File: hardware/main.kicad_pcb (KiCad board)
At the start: 2 copper layers, 60 x 40 mm, 4 parts

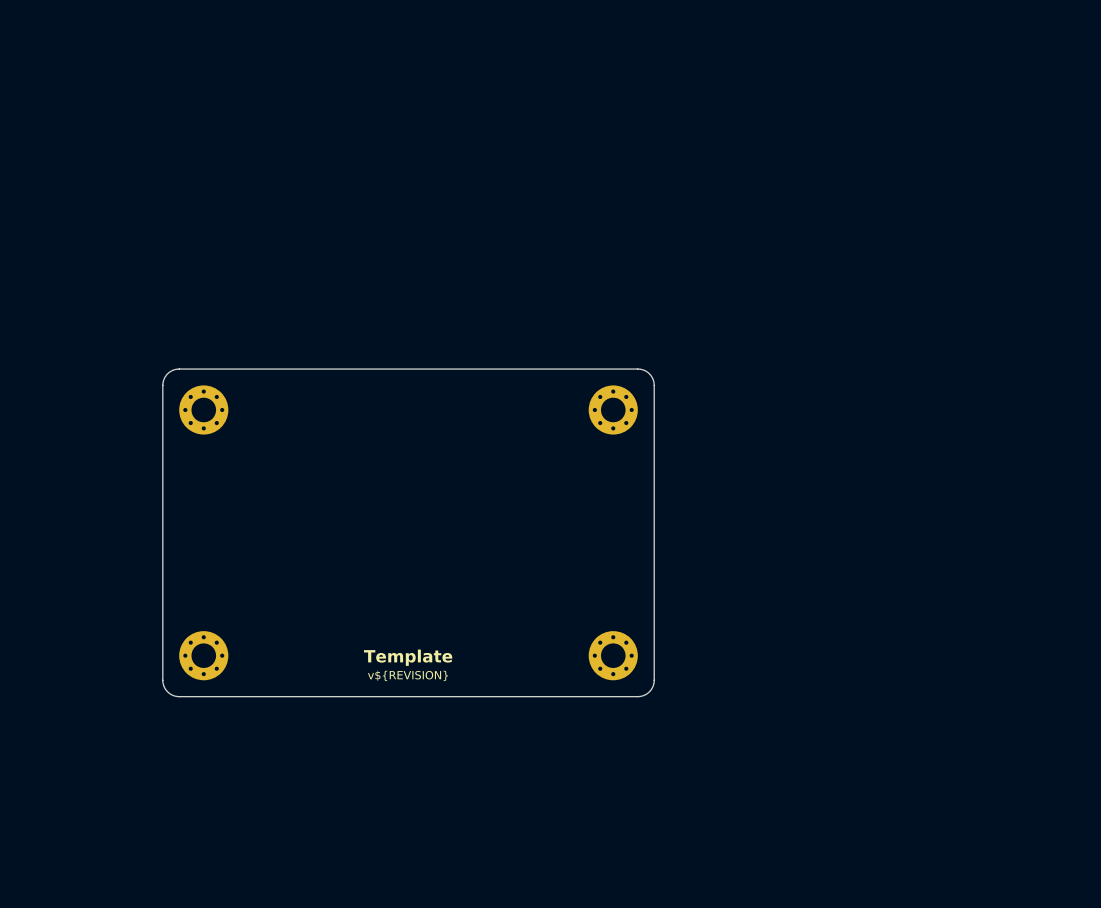
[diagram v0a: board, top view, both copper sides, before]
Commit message: add connectors and change through hole for HV
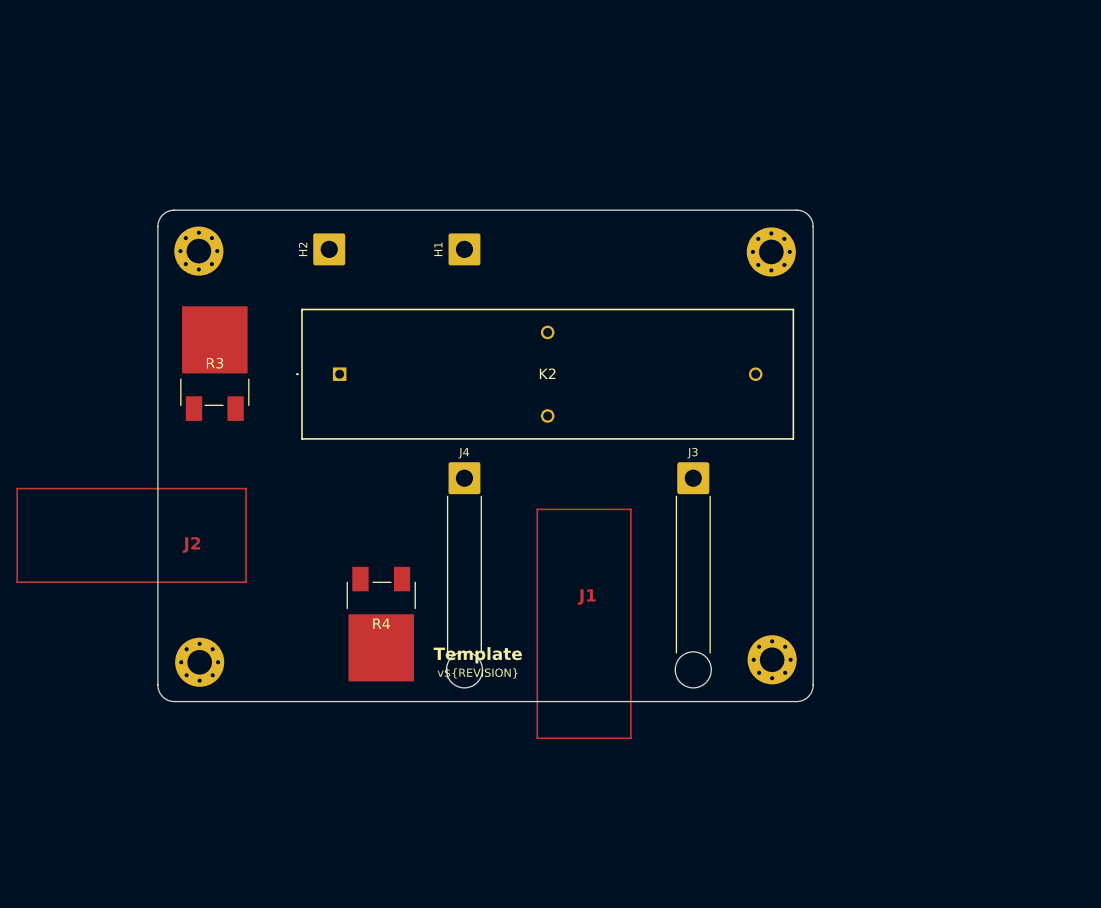
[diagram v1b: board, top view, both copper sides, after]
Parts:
- added H1: ~, Connector_Wire:SolderWire-1.5sqmm_1x01_D1.7mm_OD3.9mm, F.Cu at (152.8, 61.4)
- added H2: ~, Connector_Wire:SolderWire-1.5sqmm_1x01_D1.7mm_OD3.9mm, F.Cu at (136.3, 61.4)
- added J3: Strain_Relief_1, Connector_Wire:SolderWire-1.5sqmm_1x01_D1.7mm_OD3.9mm_Relief, F.Cu at (180.8, 89.3)
- added J4: Strain_Relief_2, Connector_Wire:SolderWire-1.5sqmm_1x01_D1.7mm_OD3.9mm_Relief, F.Cu at (152.8, 89.3)
- added K2: ADW11, KiCad:DBR72410, F.Cu at (137.6, 76.6)
- added R3: R_Small, TKH45P5K00FE-TR:TKH45P50R0FETR, F.Cu at (122.3, 76.6)
- added R4: R_Small, TKH45P5K00FE-TR:TKH45P50R0FETR, F.Cu at (142.7, 105.8)
- moved REF** 27.3 mm to (190.3, 61.7)
- moved REF** 19.4 mm to (120.4, 61.6)
- moved REF** 19.4 mm to (190.4, 111.5)
- moved REF** 0.94 mm to (120.5, 111.8)
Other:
- board size 60 x 40 mm -> 80 x 60 mm
- board text added: "J1"
- board text added: "J2"

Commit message: changed Resistors and HV Cables
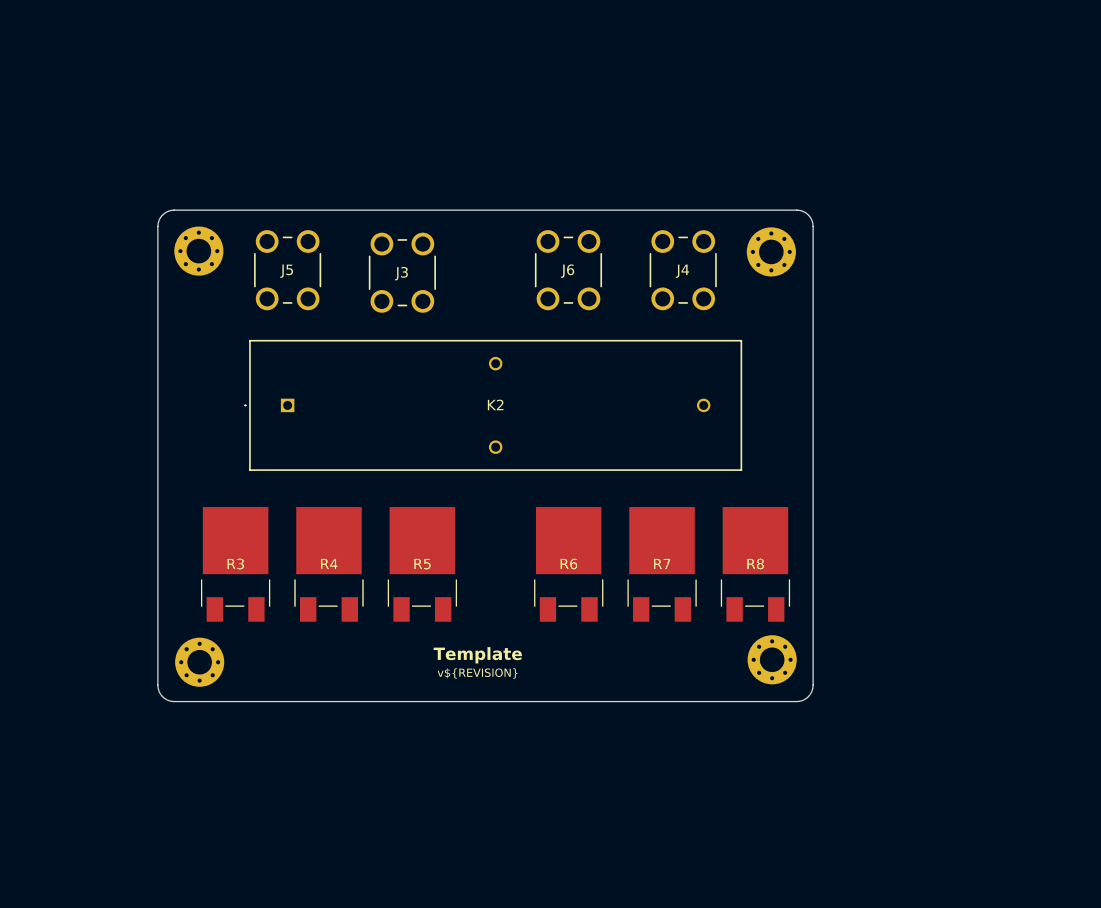
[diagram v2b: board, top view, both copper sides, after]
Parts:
- removed H1, H2: ~, Connector_Wire:SolderWire-1.5sqmm_1x01_D1.7mm_OD3.9mm
- added J5: 7696, 7696:7696, F.Cu at (128.7, 67.4)
- added J6: 7696, 7696:7696, F.Cu at (163.0, 67.4)
- added R5: TKH45P5K00FE-TR, TKH45P5K00FE-TR:TKH45P50R0FETR, F.Cu at (147.7, 101.2)
- added R6: TKH45P5K00FE-TR, TKH45P5K00FE-TR:TKH45P50R0FETR, F.Cu at (165.6, 101.2)
- added R7: TKH45P5K00FE-TR, TKH45P5K00FE-TR:TKH45P50R0FETR, F.Cu at (177.0, 101.2)
- added R8: TKH45P5K00FE-TR, TKH45P5K00FE-TR:TKH45P50R0FETR, F.Cu at (188.4, 101.2)
- J3: value Strain_Relief_1 -> 7696; footprint Connector_Wire:SolderWire-1.5sqmm_1x01_D1.7mm_OD3.9mm_Relief -> 7696:7696
- J4: value Strain_Relief_2 -> 7696; footprint Connector_Wire:SolderWire-1.5sqmm_1x01_D1.7mm_OD3.9mm_Relief -> 7696:7696
- R3, R4: value R_Small -> TKH45P5K00FE-TR
- moved J3 43.7 mm to (142.8, 67.7)
- moved J4 41.1 mm to (182.0, 60.4), turned to 180 degrees
- moved R3 24.7 mm to (124.9, 101.2)
- moved R4 7.92 mm to (136.3, 101.2), turned to 0 degrees
- moved K2 7.41 mm to (131.2, 80.4)
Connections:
- J3 pad 1: Net-(J3-Pin_1) -> Net-(J3-Pad1)
- J4 pad 1: HV+ -> Net-(J4-Pad1)
- K2 pad 1: HV- -> Net-(J6-Pad1)
- K2 pad 2: Net-(J3-Pin_1) -> Net-(J4-Pad2)
- R3 pad 1: TSMP- -> TSMP+
- R3 pad 2: HV- -> Net-(R3-Pad2)
- R3 pad 3: (no net) -> Net-(R3-Pad3)
- R4 pad 1: TSMP+ -> Net-(R3-Pad2)
- R4 pad 2: HV+ -> Net-(R4-Pad2)
- R4 pad 3: (no net) -> Net-(R3-Pad3)
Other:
- board text removed: "J1"
- board text removed: "J2"

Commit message: Still have to take the measurements
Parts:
- added J1: ~, d369-g33-xx:D369-G33-XX, F.Cu at (160.6, 66.9)
- added J2: ~, d369-g33-xx:D369-G33-XX, F.Cu at (165.5, 114.7)
- J3, J4, J5, J6: value 7696 -> Conn_01x01_Pin
- moved K2 55.9 mm to (187.1, 80.4), turned to 180 degrees
- moved J6 53.5 mm to (136.2, 113.7), turned to 180 degrees
- moved J5 48.3 mm to (177.0, 67.4)
- moved J3 46.5 mm to (147.7, 114.0), turned to 180 degrees
- moved J4 46.2 mm to (136.4, 67.4), turned to 0 degrees
- moved R8 24.2 mm to (164.3, 99.1), turned to 180 degrees
- moved R5 24.1 mm to (123.7, 99.1), turned to 180 degrees
- moved R3 21.7 mm to (146.5, 99.1), turned to 180 degrees
- moved R6 21.6 mm to (187.1, 99.1), turned to 180 degrees
- moved REF** 8.29 mm to (120.5, 120.1)
- moved REF** 8.29 mm to (190.4, 119.8)
- moved R7 2.41 mm to (175.7, 99.1), turned to 180 degrees
- moved R4 2.38 mm to (135.1, 99.1), turned to 180 degrees
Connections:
- J3 pad 1: Net-(J3-Pad1) -> HV+
- J4 pad 1: Net-(J4-Pad1) -> Net-(J4-Pin_1)
- J5 pad 1: Net-(J3-Pad1) -> HV-
- J6 pad 1: Net-(J6-Pad1) -> HV+
- K2 pad 1: Net-(J6-Pad1) -> HV-
- K2 pad 2: Net-(J4-Pad2) -> Net-(J4-Pin_1)
- R5 pad 2: Net-(J3-Pad1) -> HV+
- R8 pad 2: Net-(J6-Pad1) -> HV-
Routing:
- net GND: track 0.00 -> 21.2 mm
- net SD+: track 0.00 -> 9.91 mm
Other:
- board size 80 x 60 mm -> 80 x 68.3 mm

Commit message: Added calculations
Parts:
- moved J1 8.98 mm to (161.9, 58.0)
- moved J5 8.98 mm to (178.3, 58.5)
- moved J4 8.98 mm to (137.6, 58.5)
- moved J2 8.98 mm to (166.8, 105.8)
- moved J3 8.98 mm to (148.9, 105.1)
- moved K2 8.98 mm to (188.4, 71.5)
- moved R3 8.98 mm to (147.7, 90.2)
- moved R6 8.98 mm to (188.3, 90.2)
- moved R7 8.98 mm to (176.9, 90.2)
- moved R8 8.98 mm to (165.5, 90.2)
- moved R5 8.98 mm to (124.9, 90.2)
- moved REF** 8.98 mm to (121.7, 111.2)
- moved REF** 8.98 mm to (121.6, 52.7)
- moved R4 8.98 mm to (136.3, 90.2)
- moved REF** 8.98 mm to (191.5, 52.8)
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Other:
- outline, holes or cut-outs redrawn
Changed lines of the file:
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@@
   (net 15 "unconnected-(J2-Pin_2-Pad2)")
   (footprint "TKH45P5K00FE-TR:TKH45P50R0FETR" (layer "F.Cu")
-    (at 146.48 99.1 180)
+    (at 147.72 90.21 180)
     (descr "TKH45P50R0FE-TR-1")
     (tags "Resistor")
@@
   )
   (footprint "7696:7696" (layer "F.Cu")
-    (at 177.04 67.4295)
+    (at 178.28 58.5395)
     (descr "7696-1")
     (tags "Connector")
@@
   )
   (footprint "TKH45P5K00FE-TR:TKH45P50R0FETR" (layer "F.Cu")
-    (at 135.08 99.1 180)
+    (at 136.32 90.21 180)
     (descr "TKH45P50R0FE-TR-1")
     (tags "Resistor")
@@
   )
   (footprint "d369-g33-xx:D369-G33-XX" (layer "F.Cu")
-    (at 160.64 66.93 90)
+    (at 161.88 58.04 90)
     (descr "D369-G33-BP4-7")
     (tags "Connector")
@@
   )
   (footprint "MountingHole:MountingHole_3mm_Pad_Via" (layer "F.Cu")
-    (at 190.3 61.7)
+    (at 191.54 52.81)
     (descr "Mounting Hole 3mm")
     (tags "mounting hole 3mm")
@@
   )
   (footprint "7696:7696" (layer "F.Cu")
-    (at 136.36 67.4295)
+    (at 137.6 58.5395)
     (descr "7696-1")
     (tags "Connector")
@@
   )
   (footprint "7696:7696" (layer "F.Cu")
-    (at 147.67 114 180)
+    (at 148.91 105.11 180)
     (descr "7696-1")
     (tags "Connector")
@@
   )
   (footprint "MountingHole:MountingHole_3mm_Pad_Via" (layer "F.Cu")
-    (at 120.5 120.09)
+    (at 121.74 111.2)
     (descr "Mounting Hole 3mm")
     (tags "mounting hole 3mm")
@@
   )
   (footprint "d369-g33-xx:D369-G33-XX" (layer "F.Cu")
-    (at 165.53 114.73 -90)
+    (at 166.77 105.84 -90)
     (descr "D369-G33-BP4-7")
     (tags "Connector")
@@
   )
   (footprint "MountingHole:MountingHole_3mm_Pad_Via" (layer "F.Cu")
-    (at 120.4 61.6)
+    (at 121.64 52.71)
     (descr "Mounting Hole 3mm")
     (tags "mounting hole 3mm")
@@
   )
   (footprint "TKH45P5K00FE-TR:TKH45P50R0FETR" (layer "F.Cu")
-    (at 187.09 99.1 180)
+    (at 188.33 90.21 180)
     (descr "TKH45P50R0FE-TR-1")
     (tags "Resistor")
@@
   )
   (footprint "TKH45P5K00FE-TR:TKH45P50R0FETR" (layer "F.Cu")
-    (at 175.69 99.1 180)
+    (at 176.93 90.21 180)
     (descr "TKH45P50R0FE-TR-1")
     (tags "Resistor")
@@
   )
   (footprint "KiCad:DBR72410" (layer "F.Cu")
-    (at 187.12 80.44 180)
+    (at 188.36 71.55 180)
     (descr "DBR72410-2")
     (tags "Relay or Contactor")
@@
   )
   (footprint "MountingHole:MountingHole_3mm_Pad_Via" (layer "F.Cu")
-    (at 190.4 119.79)
+    (at 191.64 110.9)
     (descr "Mounting Hole 3mm")
     (tags "mounting hole 3mm")
@@
   )
   (footprint "TKH45P5K00FE-TR:TKH45P50R0FETR" (layer "F.Cu")
-    (at 123.68 99.1 180)
+    (at 124.92 90.21 180)
     (descr "TKH45P50R0FE-TR-1")
     (tags "Resistor")
@@
   )
   (footprint "TKH45P5K00FE-TR:TKH45P50R0FETR" (layer "F.Cu")
-    (at 164.29 99.1 180)
+    (at 165.53 90.21 180)
     (descr "TKH45P50R0FE-TR-1")
     (tags "Resistor")
@@
   )
   (footprint "7696:7696" (layer "F.Cu")
-    (at 136.2 113.6905 180)
+    (at 137.44 104.8805 180)
     (descr "7696-1")
     (tags "Connector")
@@
     )
   )
-  (gr_line (start 117.4 56.6) (end 193.4 56.6)
+  (gr_circle (center 162.96 66.47) (end 168.04 66.47)
+    (stroke (width 0.2) (type default)) (fill none) (layer "Dwgs.User"))
+  (gr_circle (center 162.96 76.63) (end 168.04 76.63)
+    (stroke (width 0.2) (type default)) (fill none) (layer "Dwgs.User"))
+  (gr_line (start 118.64 47.71) (end 194.64 47.71)
     (stroke (width 0.1) (type default)) (layer "Edge.Cuts"))
-  (gr_line (start 115.4 114.6) (end 115.4 58.6)
+  (gr_line (start 116.64 114) (end 116.64 49.71)
     (stroke (width 0.1) (type default)) (layer "Edge.Cuts"))
-  (gr_line (start 195.4 58.6) (end 195.4 122.89)
+  (gr_line (start 196.64 49.71) (end 196.64 114)
     (stroke (width 0.1) (type default)) (layer "Edge.Cuts"))
-  (gr_arc (start 117.4 124.89) (mid 115.985786 124.304214) (end 115.4 122.89)
+  (gr_arc (start 118.64 116) (mid 117.225786 115.414214) (end 116.64 114)
     (stroke (width 0.1) (type default)) (layer "Edge.Cuts"))
-  (gr_arc (start 195.4 122.89) (mid 194.814214 124.304214) (end 193.4 124.89)
+  (gr_arc (start 196.64 114) (mid 196.054214 115.414214) (end 194.64 116)
     (stroke (width 0.1) (type default)) (layer "Edge.Cuts"))
-  (gr_arc (start 115.4 58.6) (mid 115.985786 57.185786) (end 117.4 56.6)
+  (gr_arc (start 116.64 49.71) (mid 117.225786 48.295786) (end 118.64 47.71)
     (stroke (width 0.1) (type default)) (layer "Edge.Cuts"))
-  (gr_line (start 193.4 124.89) (end 117.4 124.89)
+  (gr_line (start 194.64 116) (end 118.64 116)
     (stroke (width 0.1) (type default)) (layer "Edge.Cuts"))
-  (gr_arc (start 193.4 56.6) (mid 194.814214 57.185786) (end 195.4 58.6)
+  (gr_arc (start 194.64 47.71) (mid 196.054214 48.295786) (end 196.64 49.71)
     (stroke (width 0.1) (type default)) (layer "Edge.Cuts"))
-  (gr_text "Template" (at 154.5 119.99) (layer "F.SilkS")
+  (gr_text "Template" (at 155.74 111.1) (layer "F.SilkS")
     (effects (font (size 1.5 1.5) (thickness 0.3) bold) (justify bottom))
   )
-  (gr_text "v${REVISION}" (at 154.5 121.99) (layer "F.SilkS")
+  (gr_text "v${REVISION}" (at 155.74 113.1) (layer "F.SilkS")
     (effects (font (size 1 1) (thickness 0.15)) (justify bottom))
   )
   (dimension (type aligned) (layer "Dwgs.User")
-    (pts (xy 115.4 58.6) (xy 195.4 58.6))
+    (pts (xy 162.96 76.63) (xy 162.96 66.47))
+    (height 10.16)
+    (gr_text "10.16 mm" (at 171.97 71.55 90) (layer "Dwgs.User")
+      (effects (font (size 1 1) (thickness 0.15)))
+    )
+    (format (prefix "") (suffix "") (units 3) (units_format 1) (precision 4) suppress_zeroes)
+    (style (thickness 0.2) (arrow_length 1.27) (text_position_mode 0) (extension_height 0.58642) (extension_offset 0.5) keep_text_aligned)
+  )
+  (dimension (type aligned) (layer "Dwgs.User")
+    (pts (xy 116.64 49.71) (xy 196.64 49.71))
     (height -7)
-    (gr_text "80 mm" (at 155.4 51.6) (layer "Dwgs.User")
+    (gr_text "80 mm" (at 156.64 42.71) (layer "Dwgs.User")
       (effects (font (size 1 1) (thickness 0.15)))
     )
@@
   )
   (dimension (type aligned) (layer "Dwgs.User")
-    (pts (xy 193.05 56.6) (xy 193.05 124.89))
+    (pts (xy 162.96 76.63) (xy 162.96 71.55))
+    (height -10.16)
+    (gr_text "5.08 mm" (at 151.65 74.09 90) (layer "Dwgs.User")
+      (effects (font (size 1 1) (thickness 0.15)))
+    )
+    (format (prefix "") (suffix "") (units 3) (units_format 1) (precision 4) suppress_zeroes)
+    (style (thickness 0.2) (arrow_length 1.27) (text_position_mode 0) (extension_height 0.58642) (extension_offset 0.5) keep_text_aligned)
+  )
+  (dimension (type aligned) (layer "Dwgs.User")
+    (pts (xy 194.29 47.71) (xy 194.29 116))
     (height -10.58)
-    (gr_text "68.29 mm" (at 203.63 90.745 90) (layer "Dwgs.User")
+    (gr_text "68.29 mm" (at 204.87 81.855 90) (layer "Dwgs.User")
       (effects (font (size 1 1) (thickness 0.15)))
     )
@@
     (style (thickness 0.15) (arrow_length 1.27) (text_position_mode 1) (extension_height 0.58642) (extension_offset 0.5) keep_text_aligned)
   )
-  (segment (start 155.56 79.38) (end 155.56 66.93) (width 1.3) (layer "F.Cu") (net 1))
-  (segment (start 161.72 85.54) (end 155.56 79.38) (width 1.3) (layer "F.Cu") (net 1))
-  (segment (start 161.72 72.82) (end 161.72 75.34) (width 1.3) (layer "F.Cu") (net 4))
-  (segment (start 158.1 66.93) (end 158.1 69.2) (width 1.3) (layer "F.Cu") (net 4))
-  (segment (start 158.1 69.2) (end 161.72 72.82) (width 1.3) (layer "F.Cu") (net 4))
+  (segment (start 156.8 70.49) (end 156.8 58.04) (width 1.3) (layer "F.Cu") (net 1))
+  (segment (start 162.96 76.65) (end 156.8 70.49) (width 1.3) (layer "F.Cu") (net 1))
+  (segment (start 162.96 63.93) (end 162.96 66.45) (width 1.3) (layer "F.Cu") (net 4))
+  (segment (start 159.34 58.04) (end 159.34 60.31) (width 1.3) (layer "F.Cu") (net 4))
+  (segment (start 159.34 60.31) (end 162.96 63.93) (width 1.3) (layer "F.Cu") (net 4))
   (group "" (id 423d4aa3-e0ae-4d5e-8b84-ecca8a4a8613)
     (members
